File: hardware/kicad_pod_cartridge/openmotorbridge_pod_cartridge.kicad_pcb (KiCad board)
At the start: 2 copper layers, 35 x 25 mm, 9 parts

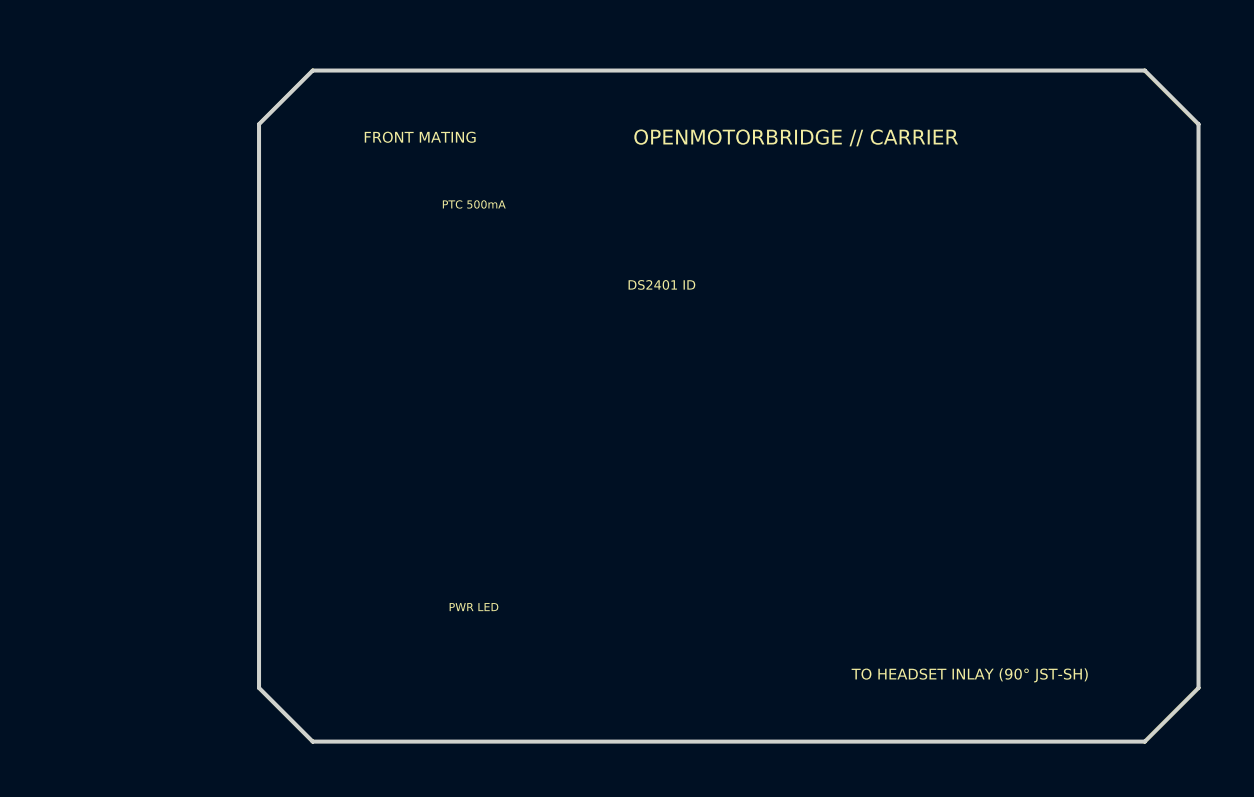
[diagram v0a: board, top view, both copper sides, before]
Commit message: Rotate J2 on Pod Cartridge PCB by 90 deg CCW (axial opening facing +X) and assign clean netlist
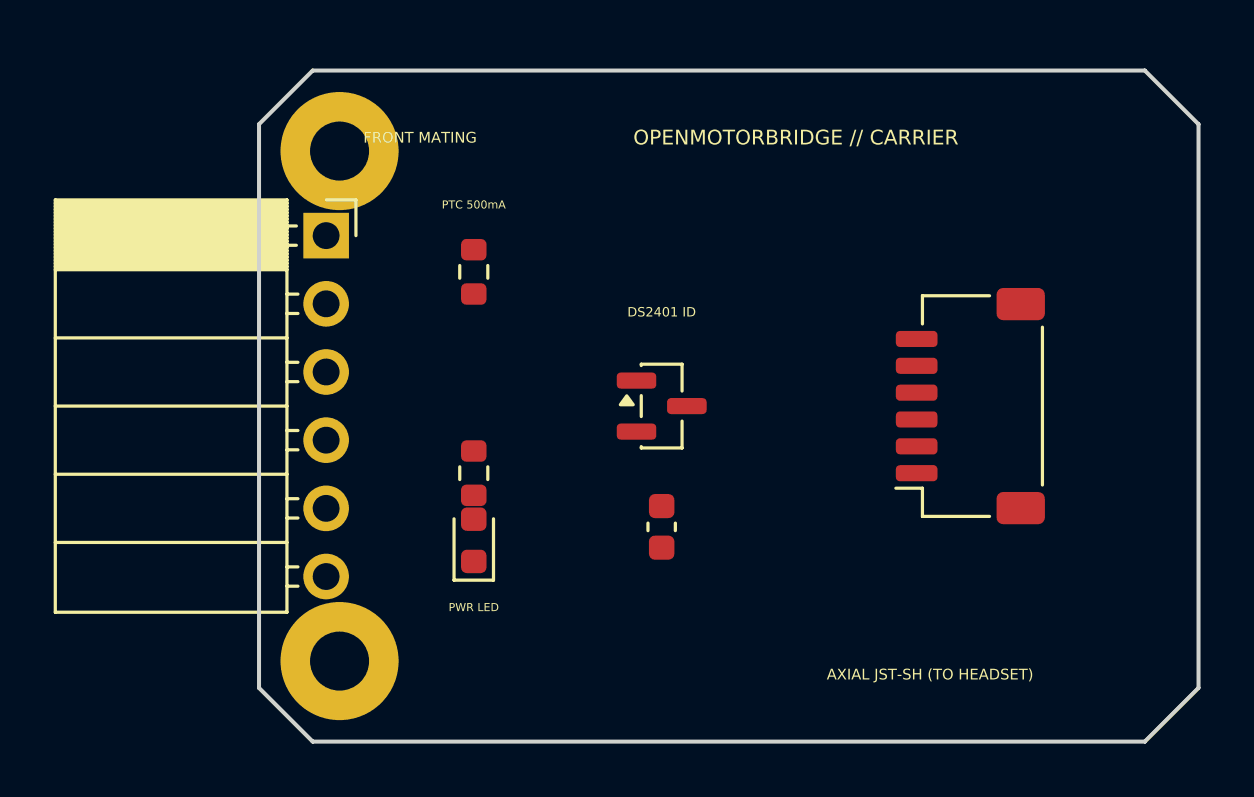
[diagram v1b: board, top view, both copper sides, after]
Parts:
- C1: value (none) -> C_0603_1608Metric; footprint (none) -> C_0603_1608Metric
- D1: value (none) -> LED_0603_1608Metric; footprint (none) -> LED_0603_1608Metric
- F1, R1: value (none) -> R_0603_1608Metric; footprint (none) -> R_0603_1608Metric
- H1, H2: value (none) -> MountingHole_2.2mm_M2_Pad; footprint (none) -> MountingHole_2.2mm_M2_Pad
- J1: value (none) -> PinSocket_1x06_P2.54mm_Horizontal; footprint (none) -> PinSocket_1x06_P2.54mm_Horizontal
- J2: value (none) -> JST_SH_SM06B-SRSS-TB_1x06-1MP_P1.00mm_Horizontal; footprint (none) -> JST_SH_SM06B-SRSS-TB_1x06-1MP_P1.00mm_Horizontal
- U1: value (none) -> SOT-23; footprint (none) -> SOT-23
- turned C1 to 90 degrees
- turned D1 to 90 degrees
- turned F1 to 90 degrees
- turned R1 to 90 degrees
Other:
- board text added: "AXIAL JST-SH (TO HEADSET)"
- board text removed: "TO HEADSET INLAY (90° JST-SH)"

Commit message: Fix netlist declarations and pad net codes for full KiCad router/autorouter connectivity
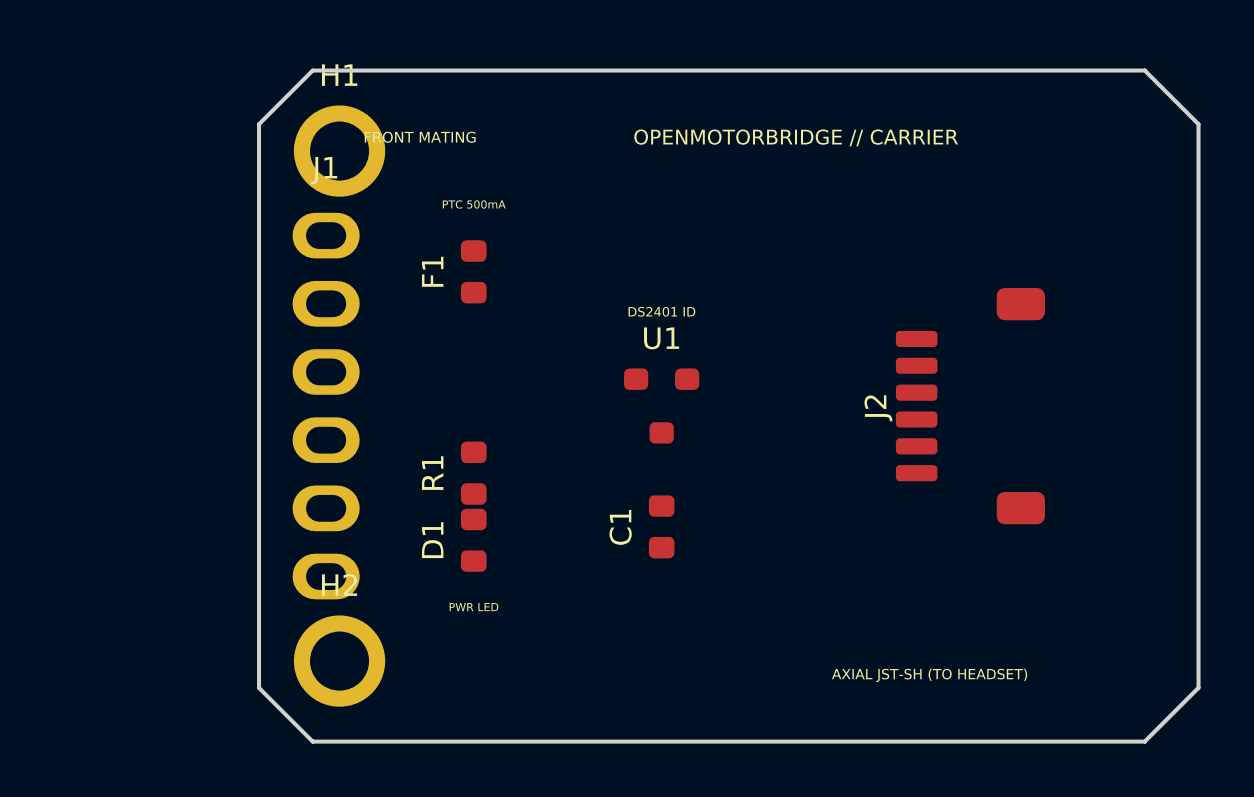
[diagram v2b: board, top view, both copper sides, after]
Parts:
- C1: value C_0603_1608Metric -> 100nF; footprint C_0603_1608Metric -> Capacitor_SMD:C_0603_1608Metric
- D1: value LED_0603_1608Metric -> GREEN_LED; footprint LED_0603_1608Metric -> LED_SMD:LED_0603_1608Metric
- F1: value R_0603_1608Metric -> PTC_500mA; footprint R_0603_1608Metric -> Resistor_SMD:R_0603_1608Metric
- H1, H2: value MountingHole_2.2mm_M2_Pad -> M2_MountingHole; footprint MountingHole_2.2mm_M2_Pad -> MountingHole:MountingHole_2.2mm_M2_Pad
- J1: value PinSocket_1x06_P2.54mm_Horizontal -> POD_BASE_SOCKET_6P; footprint PinSocket_1x06_P2.54mm_Horizontal -> Connector_PinSocket_2.54mm:PinSocket_1x06_P2.54mm_Horizontal
- J2: value JST_SH_SM06B-SRSS-TB_1x06-1MP_P1.00mm_Horizontal -> JST_SH_6P_AXIAL; footprint JST_SH_SM06B-SRSS-TB_1x06-1MP_P1.00mm_Horizontal -> Connector_JST:JST_SH_SM06B-SRSS-TB_1x06-1MP_P1.00mm_Horizontal
- R1: value R_0603_1608Metric -> 1.5k; footprint R_0603_1608Metric -> Resistor_SMD:R_0603_1608Metric
- U1: value SOT-23 -> DS2401; footprint SOT-23 -> Package_TO_SOT_SMD:SOT-23
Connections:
- J2 pad 1: GND -> VCC_5V_PROT
- J2 pad 2: VCC_5V_PROT -> POD_NF_P
- J2 pad 3: POD_NF_P -> POD_NF_N
- J2 pad 4: POD_NF_N -> POD_OPTO_KEY
- J2 pad 6: POD_OPTO_KEY -> GND
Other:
- rule pad_to_mask_clearance: 0 -> 0.05

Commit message: Update docs with 2-piece modular cartridge architecture, sealing specs, and 1:1:1 Pod 3 assembly CAD visualizations
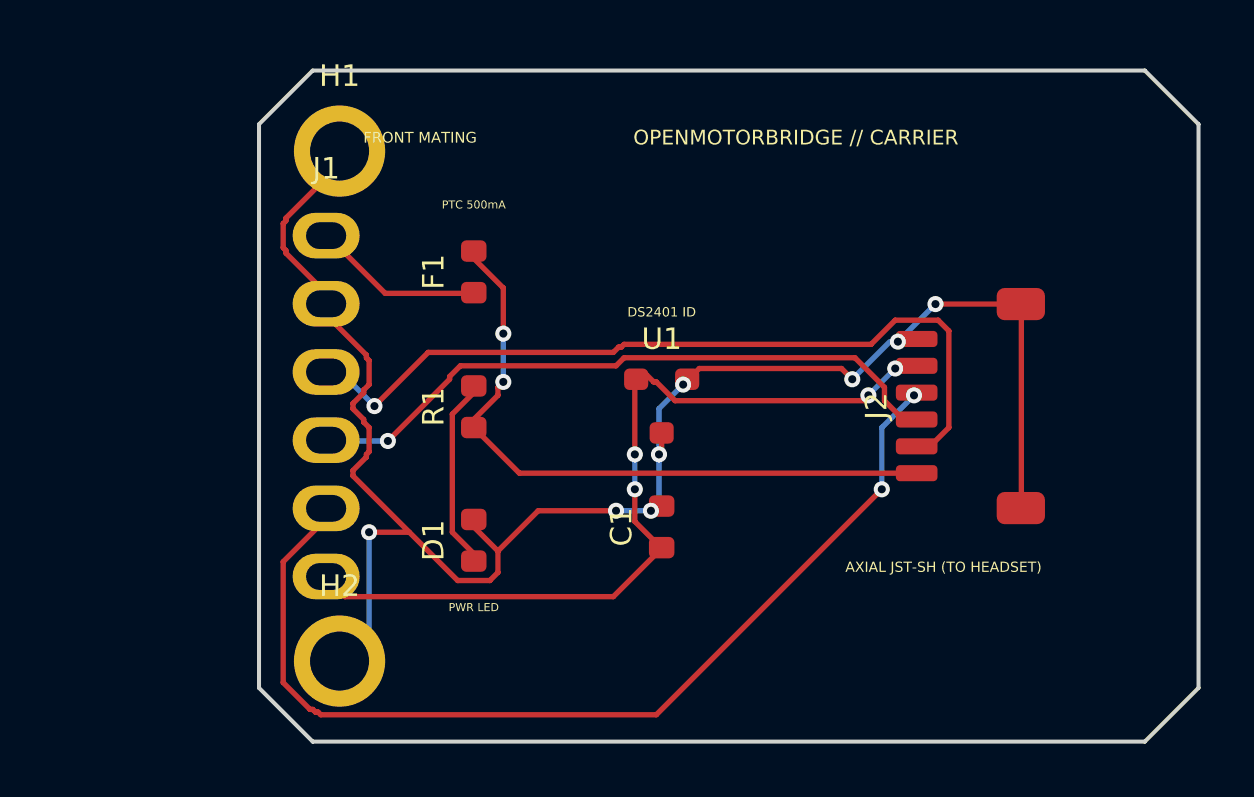
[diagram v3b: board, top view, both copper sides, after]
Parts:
- moved R1 2.47 mm to (108.0, 80.0)
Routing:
- net GND: track 0.00 -> 65.1 mm, vias 0 -> 8
- net POD_OPTO_KEY: track 0.00 -> 37.0 mm, vias 0 -> 2
- net POD_1WIRE_ID: track 0.00 -> 31.7 mm, vias 0 -> 4
- net POD_NF_P: track 0.00 -> 29.8 mm, vias 0 -> 1
- net VCC_5V_PROT: track 0.00 -> 24.7 mm, vias 0 -> 2
- net POD_NF_N: track 0.00 -> 24.6 mm, vias 0 -> 1
- net NET_LED_R: track 0.00 -> 7.34 mm
- net POD_VCC: track 0.00 -> 6.44 mm

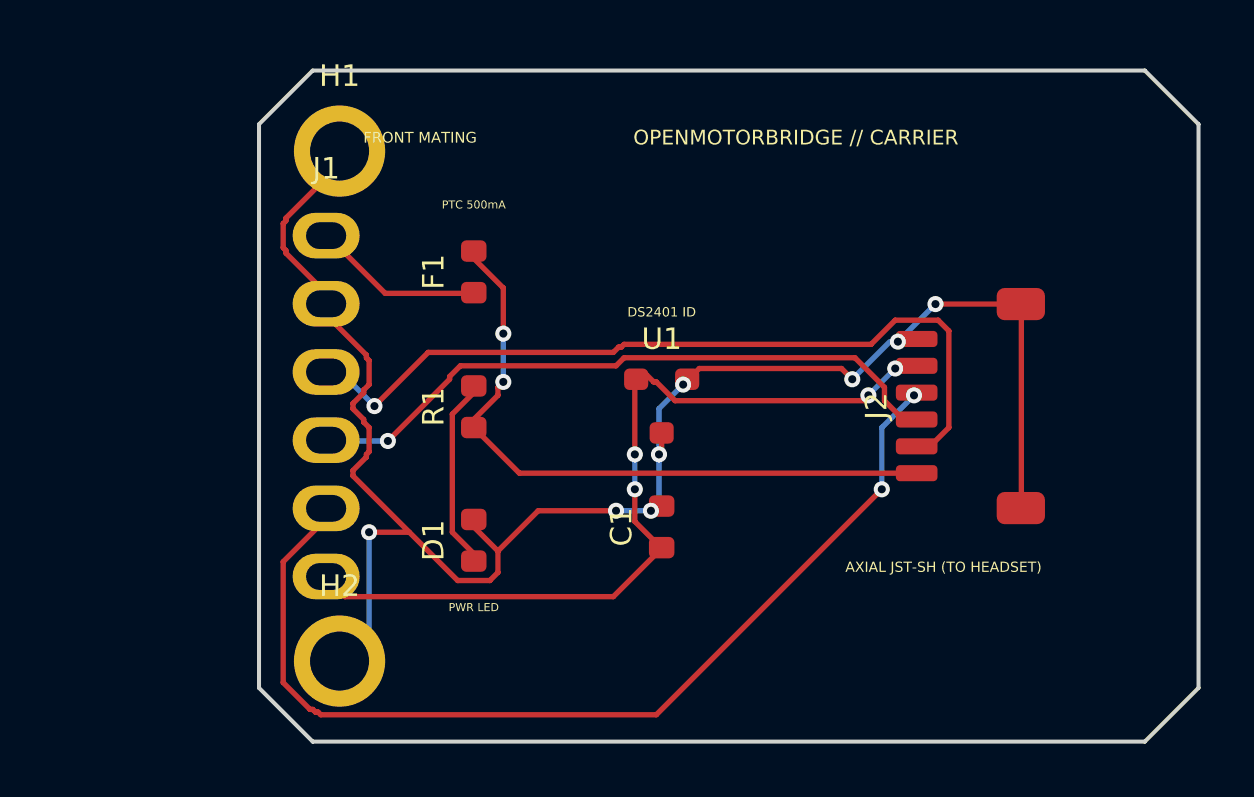
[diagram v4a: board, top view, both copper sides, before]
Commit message: Clean dangling stubs on Rear Pod 3 D1 GND and Pod Cartridge D+ audio traces, update 3D renders
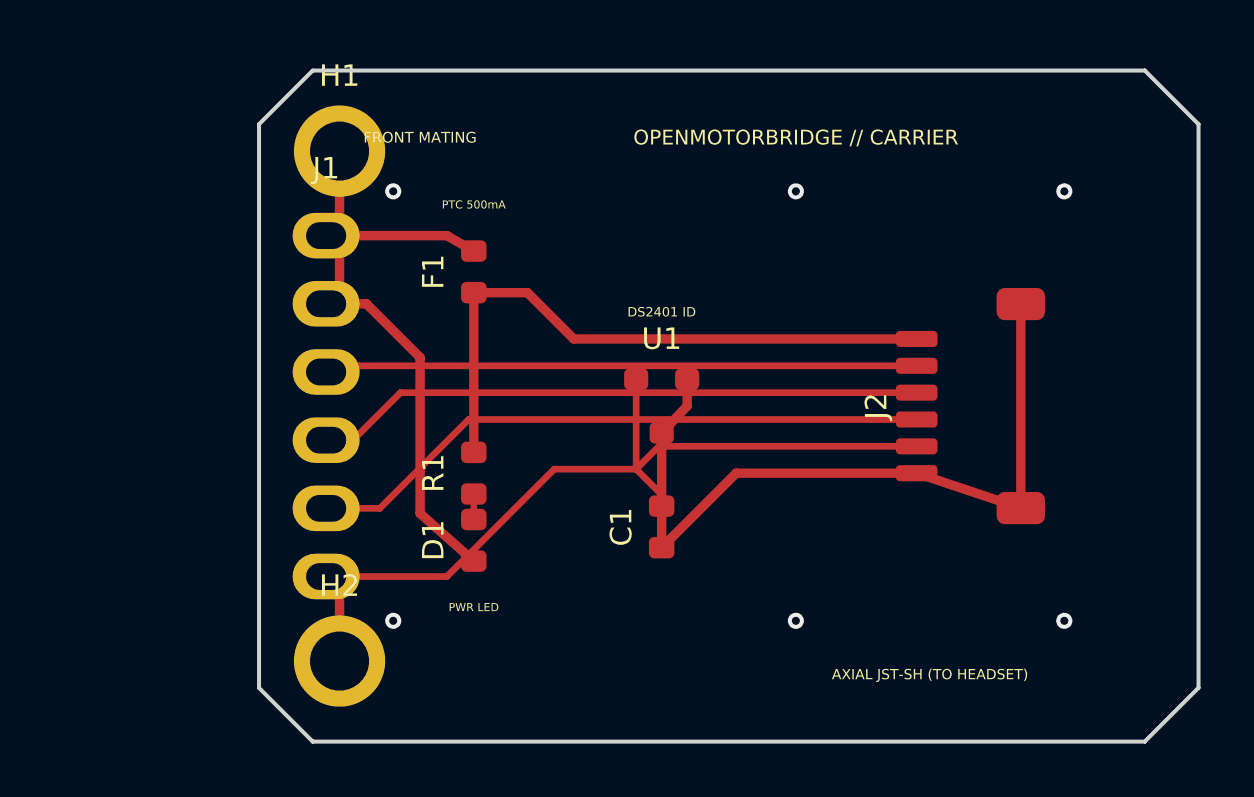
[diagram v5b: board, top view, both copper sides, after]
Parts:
- moved R1 2.47 mm to (108.0, 82.5)
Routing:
- net GND: track 65.1 -> 51.1 mm, vias 8 -> 6
- net POD_OPTO_KEY: track 37.0 -> 23.4 mm, vias 2 -> 0
- net POD_NF_P: track 29.8 -> 22.1 mm, vias 1 -> 0
- net NET_LED_R: track 7.34 -> 0.95 mm
- net POD_1WIRE_ID: track 31.7 -> 29.1 mm, vias 4 -> 0
- net POD_NF_N: track 24.6 -> 22.7 mm, vias 1 -> 0
- net VCC_5V_PROT: track 24.7 -> 23.2 mm, vias 2 -> 0
- net POD_VCC: track 6.44 -> 5.65 mm

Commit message: feat(hardware): finalize JLCPCB-compliant autorouting across all 4 PCBs
- Configure JLCPCB standard net classes ('Default' & 'Power') in .kicad_pro and .kicad_pcb
- Set board setup constraints: 0.15/0.20mm trace, 0.60/0.30mm via, 0.127/0.15mm clearance
- Complete 100% autorouting for Main Board, Pod Base, Pod Cartridge, and Rear Pod 3
- Eliminate manual 2D trace generation scripts and planar crossing errors
- Update verification tool (verify_pcb_designs_jlcpcb.py) to audit 2-layer and 4-layer capabilities
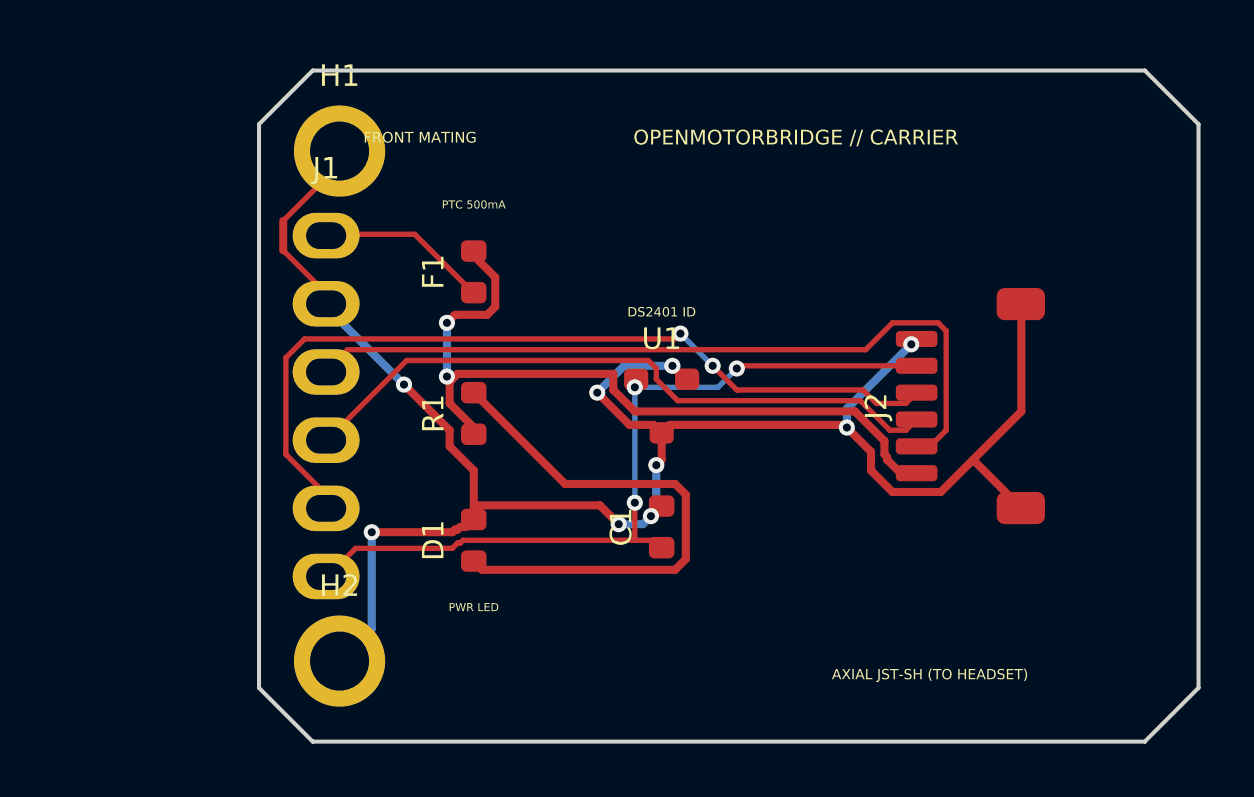
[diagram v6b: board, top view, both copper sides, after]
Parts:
- moved R1 2.22 mm to (108.0, 80.3)
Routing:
- net GND: track 51.1 -> 70.9 mm, vias 6 -> 9
- net NET_LED_R: track 0.95 -> 20.1 mm
- net POD_OPTO_KEY: track 23.4 -> 30.8 mm, vias 0 -> 2
- net POD_NF_P: track 22.1 -> 29.0 mm
- net VCC_5V_PROT: track 23.2 -> 28.7 mm, vias 0 -> 2
- net POD_NF_N: track 22.7 -> 24.7 mm
- net POD_1WIRE_ID: track 29.1 -> 30.0 mm, vias 0 -> 3
- net POD_VCC: track 5.65 -> 6.44 mm

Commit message: feat(cad): export validated STLs, 3D renders and manufacturing packages with verified hole coordinates
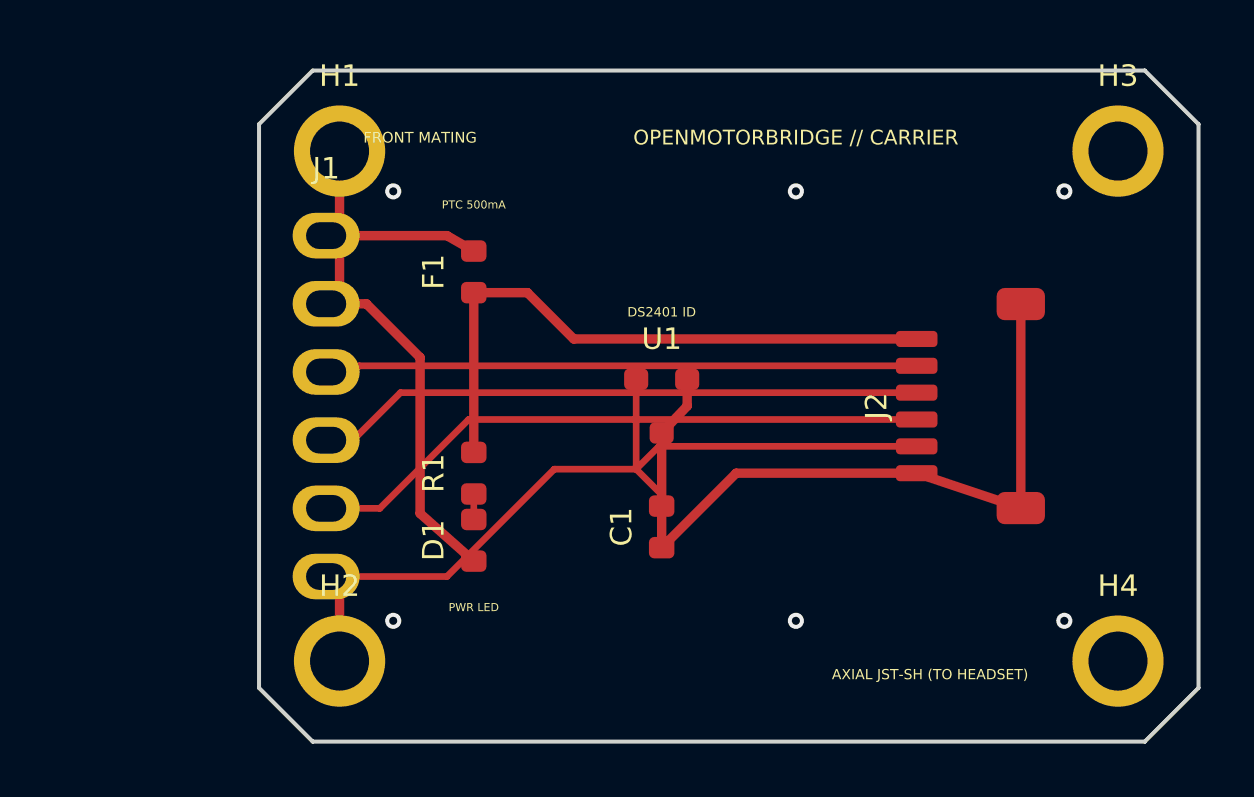
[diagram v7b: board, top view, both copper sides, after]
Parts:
- added H3: M2_MountingHole, MountingHole:MountingHole_2.2mm_M2_Pad, F.Cu at (132.0, 70.5)
- added H4: M2_MountingHole, MountingHole:MountingHole_2.2mm_M2_Pad, F.Cu at (132.0, 89.5)
- moved R1 2.22 mm to (108.0, 82.5)
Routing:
- net GND: track 70.9 -> 51.1 mm, vias 9 -> 6
- net NET_LED_R: track 20.1 -> 0.95 mm
- net POD_OPTO_KEY: track 30.8 -> 23.4 mm, vias 2 -> 0
- net POD_NF_P: track 29.0 -> 22.1 mm
- net VCC_5V_PROT: track 28.7 -> 23.2 mm, vias 2 -> 0
- net POD_NF_N: track 24.7 -> 22.7 mm
- net POD_1WIRE_ID: track 30.0 -> 29.1 mm, vias 3 -> 0
- net POD_VCC: track 6.44 -> 5.65 mm
